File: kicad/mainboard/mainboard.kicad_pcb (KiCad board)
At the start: 2 copper layers, 190.5 x 66 mm, 146 parts, among them J1 +12V BATTERY, J11 Conn_02x12, J12 Conn 02x03, J2 REMOTE INPUT, J3 LINK INPUT, J4 MIC INPUT, J5 LINE INPUT, J6 OUTPUT A, J7 OUTPUT B, J8 VDC INPUT, J9 RADIO INTERFACE, T1 IRL520N, T2 IRL520N, T3 IRF9Z24, T4 IRL520N, T5 IRL520N, T6 IRF9Z24, U1 ATMEGA16/32-P, U10 LM358N, U11 7809TV, U12 7809TV, U13 7805TV, U14 LM2941T, U2 LM324N, U4 LM358N, U8 LTC1661, U9 MAX232

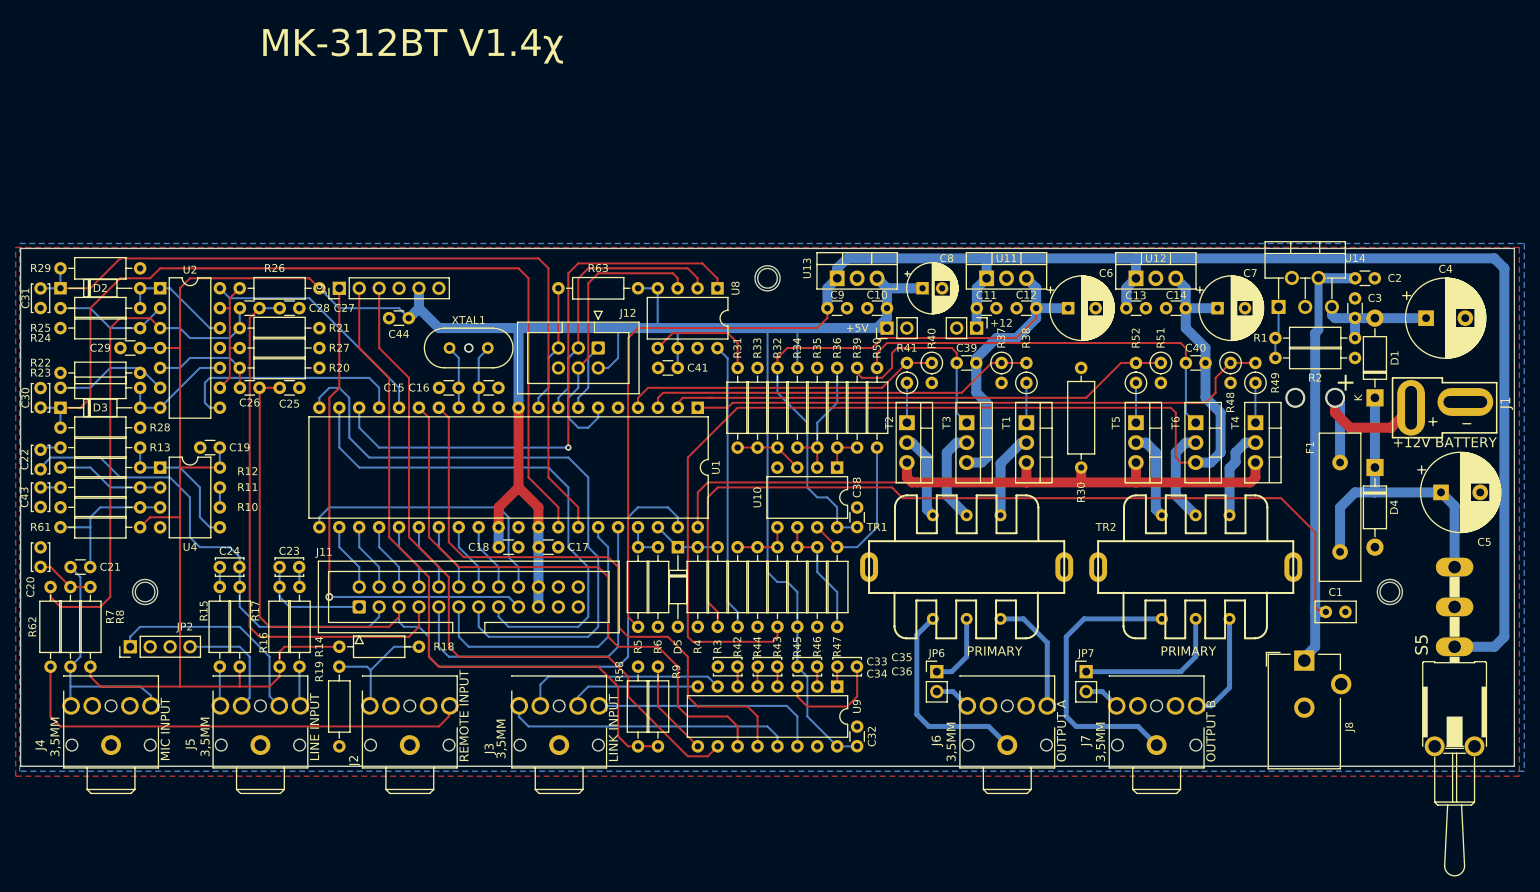
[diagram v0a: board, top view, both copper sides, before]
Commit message: Putting in new combined footprint for transformer. Updated F.Fab layer with component values in the correct place
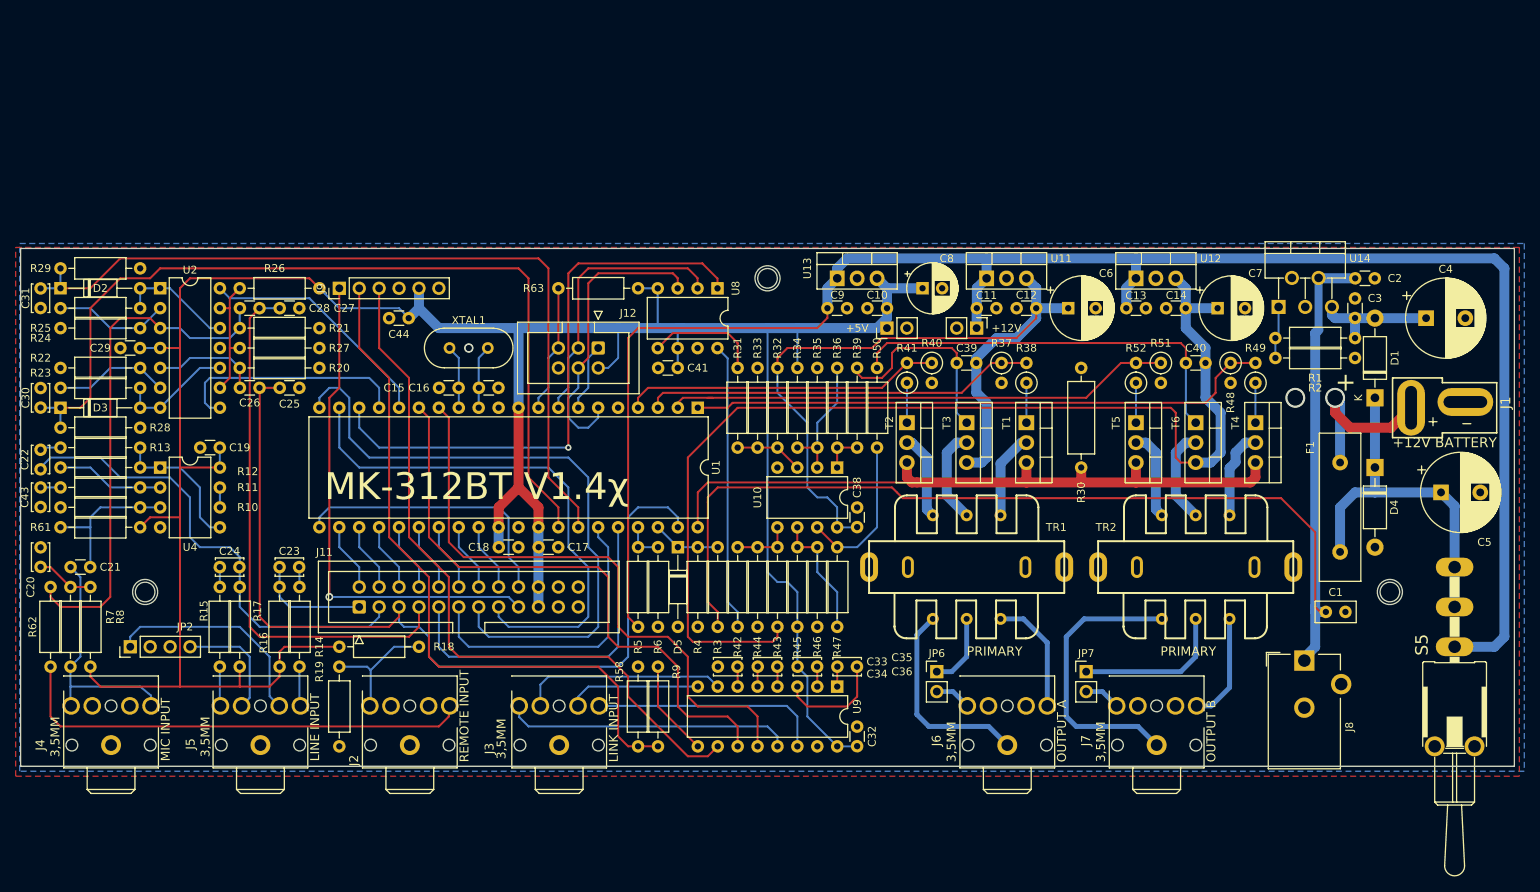
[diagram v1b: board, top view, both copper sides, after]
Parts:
- JP4: value +12 -> +12V
- TR1, TR2: footprint mk312:Transformer_Xicon_42TU -> mk312:Transformer_Xicon_42TL_42TU_Combi
- moved R22 0.63 mm to (55.9, 66.0)
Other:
- board text removed: "16V"
- board text removed: "25V"
- board text removed: "6.3V"

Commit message: Fixed footprint for powerbus connector. Bumped version to 1.4.1.
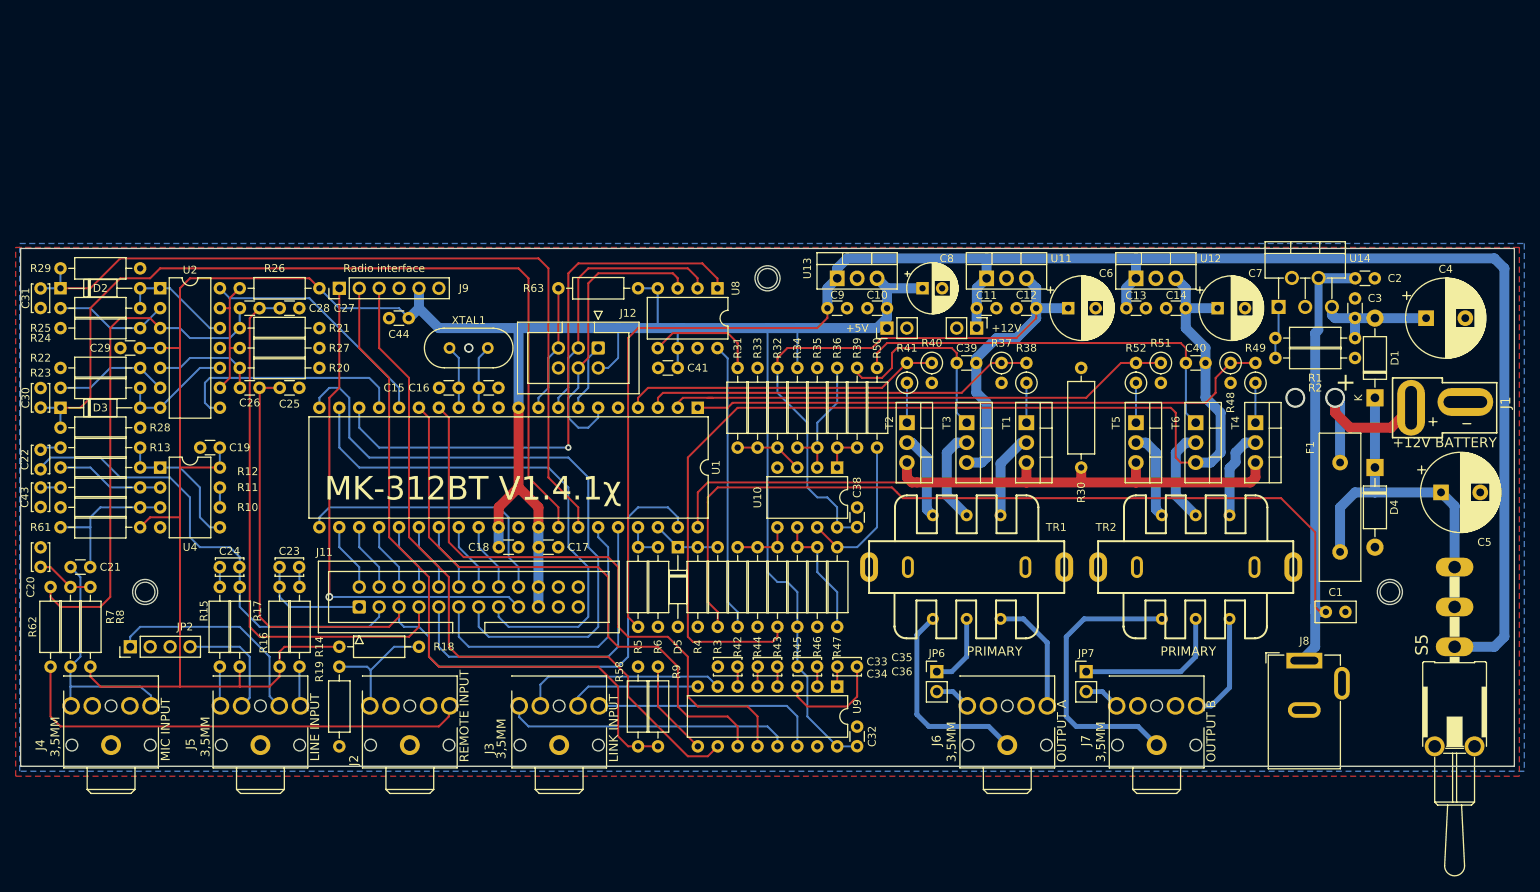
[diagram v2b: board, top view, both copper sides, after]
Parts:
- J8: footprint Connector_BarrelJack:BarrelJack_CUI_PJ-102AH_Horizontal -> Connector_BarrelJack:BarrelJack_GCT_DCJ200-10-A_Horizontal
- R30: value 0.27R -> 0.5R
- TR1, TR2: value 42TU200 -> 42TL004
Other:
- board text added: "MK-312BT V1.4.1χ"
- board text removed: "MK-312BT V1.4χ"
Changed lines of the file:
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@@
   (title_block
     (title "MK312-BT Mainboard")
-    (date "2022-08-01")
-    (rev "1.3.1-Chi")
+    (date "2022-09-04")
+    (rev "1.4.1-Chi")
   )
   (layers
@@
       (usegerberextensions true)
       (usegerberattributes false)
-      (usegerberadvancedattributes true)
+      (usegerberadvancedattributes false)
       (creategerberjobfile false)
       (svguseinch false)
@@
     (property "Sheetname" "CPU & link")
     (attr through_hole)
-    (fp_text reference "J9" (at 0 -2.33 90) (layer "F.SilkS")
+    (fp_text reference "J9" (at 0 15.875 180) (layer "F.SilkS")
       (effects (font (size 1 1) (thickness 0.15)))
     )
@@
       (effects (font (size 1 1) (thickness 0.15)))
     )
+    (fp_text user "Radio interface" (at 2.54 5.715 unlocked) (layer "F.SilkS")
+      (effects (font (size 1 1) (thickness 0.15)))
+    )
     (fp_text user "${REFERENCE}" (at 0 15.24 90) (layer "F.Fab")
       (effects (font (size 1 1) (thickness 0.15)))
@@
       (effects (font (size 1 1) (thickness 0.15)))
     )
-    (fp_text value "0.27R" (at 6.35 0 90) (layer "F.Fab")
+    (fp_text value "0.5R" (at 6.35 0 90) (layer "F.Fab")
       (effects (font (size 1 1) (thickness 0.15)))
     )
@@
     )
   )
-  (footprint "Connector_BarrelJack:BarrelJack_CUI_PJ-102AH_Horizontal" (layer "F.Cu")
+  (footprint "Connector_BarrelJack:BarrelJack_GCT_DCJ200-10-A_Horizontal" (layer "F.Cu")
     (at 214.515 103.365)
-    (descr "Thin-pin DC Barrel Jack, https://cdn-shop.adafruit.com/datasheets/21mmdcjackDatasheet.pdf")
-    (tags "Power Jack")
+    (descr "Barrel jack connector (5.5 mm outer diameter, 2.05 inner diameter ), https://gct.co/files/drawings/dcj200-10.pdf")
+    (tags "connector barrel jack")
     (property "Sheetfile" "PSU.kicad_sch")
     (property "Sheetname" "PSU")
     (attr through_hole)
-    (fp_text reference "J8" (at 5.75 8.45 90) (layer "F.SilkS")
+    (fp_text reference "J8" (at 0 -2.5) (layer "F.SilkS")
       (effects (font (size 1 1) (thickness 0.15)))
     )
-    (fp_text value "VDC INPUT" (at -5.5 6.2 90) (layer "F.Fab")
+    (fp_text value "VDC INPUT" (at 0 15.5) (layer "F.Fab")
       (effects (font (size 1 1) (thickness 0.15)))
     )
-    (fp_text user "${REFERENCE}" (at 0 6.5) (layer "F.Fab")
+    (fp_text user "${REFERENCE}" (at 0 3) (layer "F.Fab")
       (effects (font (size 1 1) (thickness 0.15)))
     )
-    (fp_line (start -4.84 -1.04) (end -3.1 -1.04) (layer "F.SilkS") (width 0.12))
-    (fp_line (start 4.6 4.8) (end 4.6 13.8) (layer "F.SilkS") (width 0.12))
-    (fp_line (start 1.8 -0.8) (end 4.6 -0.8) (layer "F.SilkS") (width 0.12))
-    (fp_line (start -4.84 0.7) (end -4.84 -1.04) (layer "F.SilkS") (width 0.12))
+    (fp_line (start 2.6 -0.7) (end 4.6 -0.7) (layer "F.SilkS") (width 0.12))
+    (fp_line (start -3.2 -1) (end -4.9 -1) (layer "F.SilkS") (width 0.12))
+    (fp_line (start 4.6 -0.7) (end 4.6 0.6) (layer "F.SilkS") (width 0.12))
+    (fp_line (start -4.6 13.8) (end -4.6 -0.7) (layer "F.SilkS") (width 0.12))
+    (fp_line (start -4.9 -1) (end -4.9 0.3) (layer "F.SilkS") (width 0.12))
+    (fp_line (start 4.6 5.2) (end 4.6 13.8) (layer "F.SilkS") (width 0.12))
+    (fp_line (start -4.6 -0.7) (end -2.6 -0.7) (layer "F.SilkS") (width 0.12))
     (fp_line (start 4.6 13.8) (end -4.6 13.8) (layer "F.SilkS") (width 0.12))
-    (fp_line (start 4.6 -0.8) (end 4.6 1.2) (layer "F.SilkS") (width 0.12))
-    (fp_line (start -4.6 -0.8) (end -1.8 -0.8) (layer "F.SilkS") (width 0.12))
-    (fp_line (start -4.6 13.8) (end -4.6 -0.8) (layer "F.SilkS") (width 0.12))
-    (fp_line (start 1.8 -1.2) (end 5 -1.2) (layer "F.CrtYd") (width 0.05))
-    (fp_line (start 5 1.2) (end 6.5 1.2) (layer "F.CrtYd") (width 0.05))
-    (fp_line (start 1.8 -1.8) (end 1.8 -1.2) (layer "F.CrtYd") (width 0.05))
-    (fp_line (start -1.8 -1.8) (end 1.8 -1.8) (layer "F.CrtYd") (width 0.05))
-    (fp_line (start 5 14.2) (end -5 14.2) (layer "F.CrtYd") (width 0.05))
-    (fp_line (start -1.8 -1.2) (end -1.8 -1.8) (layer "F.CrtYd") (width 0.05))
-    (fp_line (start -5 -1.2) (end -1.8 -1.2) (layer "F.CrtYd") (width 0.05))
-    (fp_line (start 5 4.8) (end 5 14.2) (layer "F.CrtYd") (width 0.05))
-    (fp_line (start -5 14.2) (end -5 -1.2) (layer "F.CrtYd") (width 0.05))
-    (fp_line (start 6.5 4.8) (end 5 4.8) (layer "F.CrtYd") (width 0.05))
-    (fp_line (start 5 -1.2) (end 5 1.2) (layer "F.CrtYd") (width 0.05))
-    (fp_line (start 6.5 1.2) (end 6.5 4.8) (layer "F.CrtYd") (width 0.05))
-    (fp_line (start 4.5 -0.7) (end 4.5 13.7) (layer "F.Fab") (width 0.1))
-    (fp_line (start -4.5 0.3) (end -3.5 -0.7) (layer "F.Fab") (width 0.1))
-    (fp_line (start -3.5 -0.7) (end 4.5 -0.7) (layer "F.Fab") (width 0.1))
+    (fp_line (start 5 14.2) (end 5 5.5) (layer "F.CrtYd") (width 0.05))
+    (fp_line (start 6.3 0.3) (end 6.3 5.5) (layer "F.CrtYd") (width 0.05))
+    (fp_line (start -5 14.2) (end 5 14.2) (layer "F.CrtYd") (width 0.05))
+    (fp_line (start -5 -1.5) (end -5 14.2) (layer "F.CrtYd") (width 0.05))
+    (fp_line (start 6.3 0.3) (end 5 0.3) (layer "F.CrtYd") (width 0.05))
+    (fp_line (start 5 -1.5) (end -5 -1.5) (layer "F.CrtYd") (width 0.05))
+    (fp_line (start 6.3 5.5) (end 5 5.5) (layer "F.CrtYd") (width 0.05))
+    (fp_line (start 5 0.3) (end 5 -1.5) (layer "F.CrtYd") (width 0.05))
+    (fp_line (start 4.5 -0.6) (end -3.5 -0.6) (layer "F.Fab") (width 0.1))
+    (fp_line (start -4.5 13.7) (end -4.5 0.4) (layer "F.Fab") (width 0.1))
     (fp_line (start 4.5 13.7) (end -4.5 13.7) (layer "F.Fab") (width 0.1))
-    (fp_line (start -4.5 13.7) (end -4.5 0.3) (layer "F.Fab") (width 0.1))
-    (fp_line (start -4.5 10.2) (end 4.5 10.2) (layer "F.Fab") (width 0.1))
-    (pad "1" thru_hole rect (at 0 0) (size 2.6 2.6) (drill 1.6) (layers *.Cu *.Mask)
+    (fp_line (start -4.5 0.4) (end -3.5 -0.6) (layer "F.Fab") (width 0.1))
+    (fp_line (start 4.5 -0.6) (end 4.5 13.7) (layer "F.Fab") (width 0.1))
+    (pad "1" thru_hole rect (at 0 0) (size 4.6 2) (drill oval 3.6 1) (layers *.Cu *.Mask)
       (net 1 "+VDC") (pintype "passive"))
-    (pad "2" thru_hole circle (at 0 6) (size 2.6 2.6) (drill 1.6) (layers *.Cu *.Mask)
+    (pad "2" thru_hole oval (at 0 6.3) (size 4.2 2) (drill oval 3.2 1) (layers *.Cu *.Mask)
       (net 2 "GND") (pintype "passive"))
-    (pad "3" thru_hole circle (at 4.7 3) (size 2.6 2.6) (drill 1.6) (layers *.Cu *.Mask)
+    (pad "3" thru_hole oval (at 4.8 2.9) (size 2 4.2) (drill oval 1 3.2) (layers *.Cu *.Mask)
       (net 2 "GND") (pintype "passive"))
-    (model "${KICAD6_3DMODEL_DIR}/Connector_BarrelJack.3dshapes/BarrelJack_CUI_PJ-102AH_Horizontal.wrl"
+    (model "${KICAD6_3DMODEL_DIR}/Connector_BarrelJack.3dshapes/BarrelJack_GCT_DCJ200-10-A_Horizontal.wrl"
       (offset (xyz 0 0 0))
       (scale (xyz 1 1 1))
@@
       (effects (font (size 1 1) (thickness 0.15)))
     )
-    (fp_text value "42TU200" (at 0 3.302 unlocked) (layer "F.Fab")
+    (fp_text value "42TL004" (at 0 3.302 unlocked) (layer "F.Fab")
       (effects (font (size 1 1) (thickness 0.15)))
     )
@@
       (effects (font (size 1 1) (thickness 0.15)))
     )
-    (fp_text value "42TU200" (at 0 3.302 unlocked) (layer "F.Fab")
+    (fp_text value "42TL004" (at 0 3.302 unlocked) (layer "F.Fab")
       (effects (font (size 1 1) (thickness 0.15)))
     )
@@
     (effects (font (size 2.3368 2.3368) (thickness 0.2032)) (justify left bottom))
   )
-  (gr_text "MK-312BT V1.4χ" (at 89.535 83.185) (layer "F.SilkS")
-    (effects (font (size 3.429 3.429) (thickness 0.381)) (justify left bottom))
+  (gr_text "MK-312BT V1.4.1χ" (at 89.535 83.185) (layer "F.SilkS")
+    (effects (font (size 3 3) (thickness 0.381)) (justify left bottom))
   )
   (gr_text "PRIMARY" (at 196.153369 102.87) (layer "F.SilkS")
